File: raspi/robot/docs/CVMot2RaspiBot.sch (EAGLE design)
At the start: 2 parts

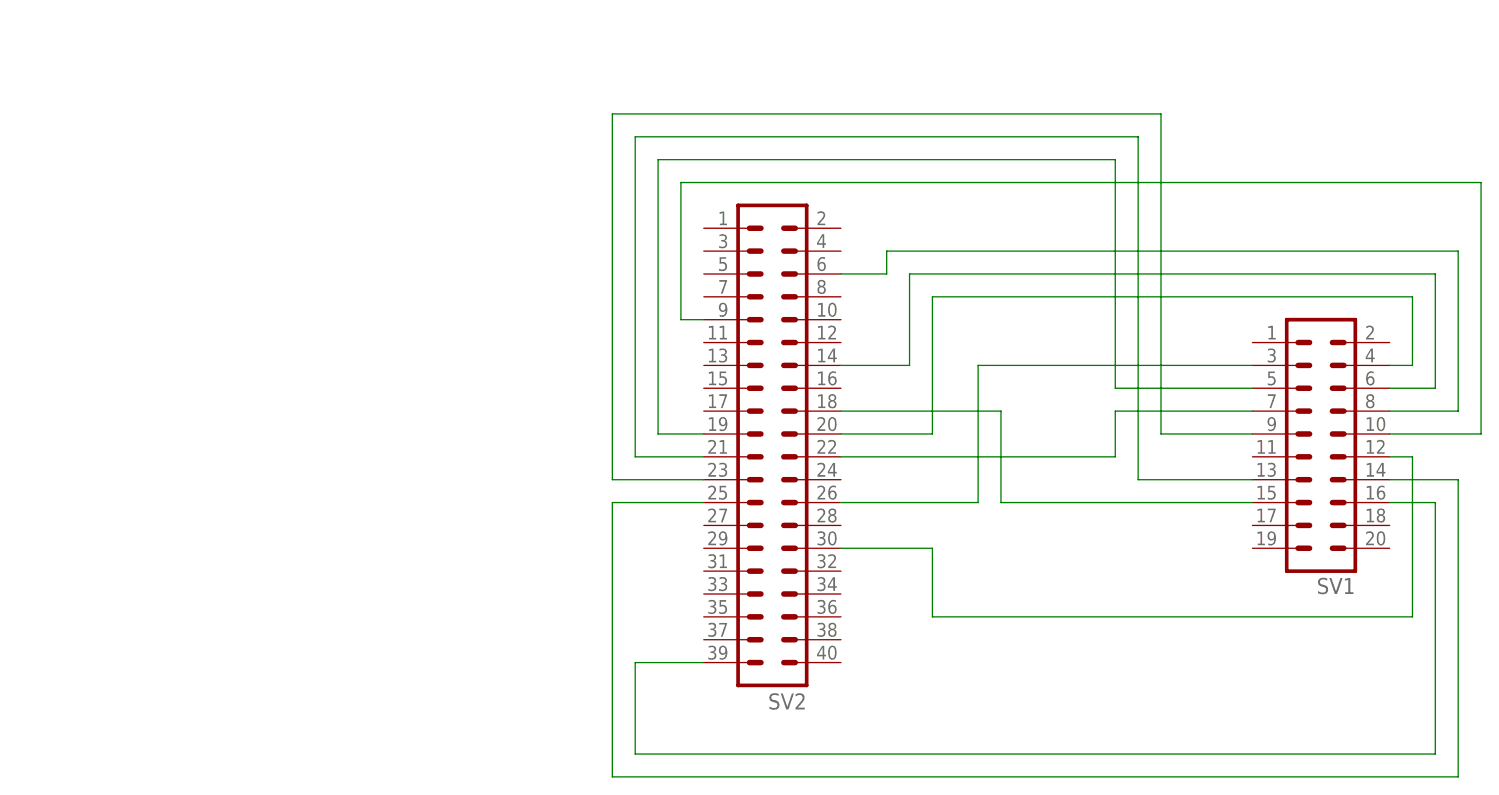
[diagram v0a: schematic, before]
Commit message: Raspi: Neue Adapter-Schaltpläne
git-svn-id: https://cvsvn/svn/raspi/trunk@92 50237d99-7d21-444e-87dd-016511c29f8c
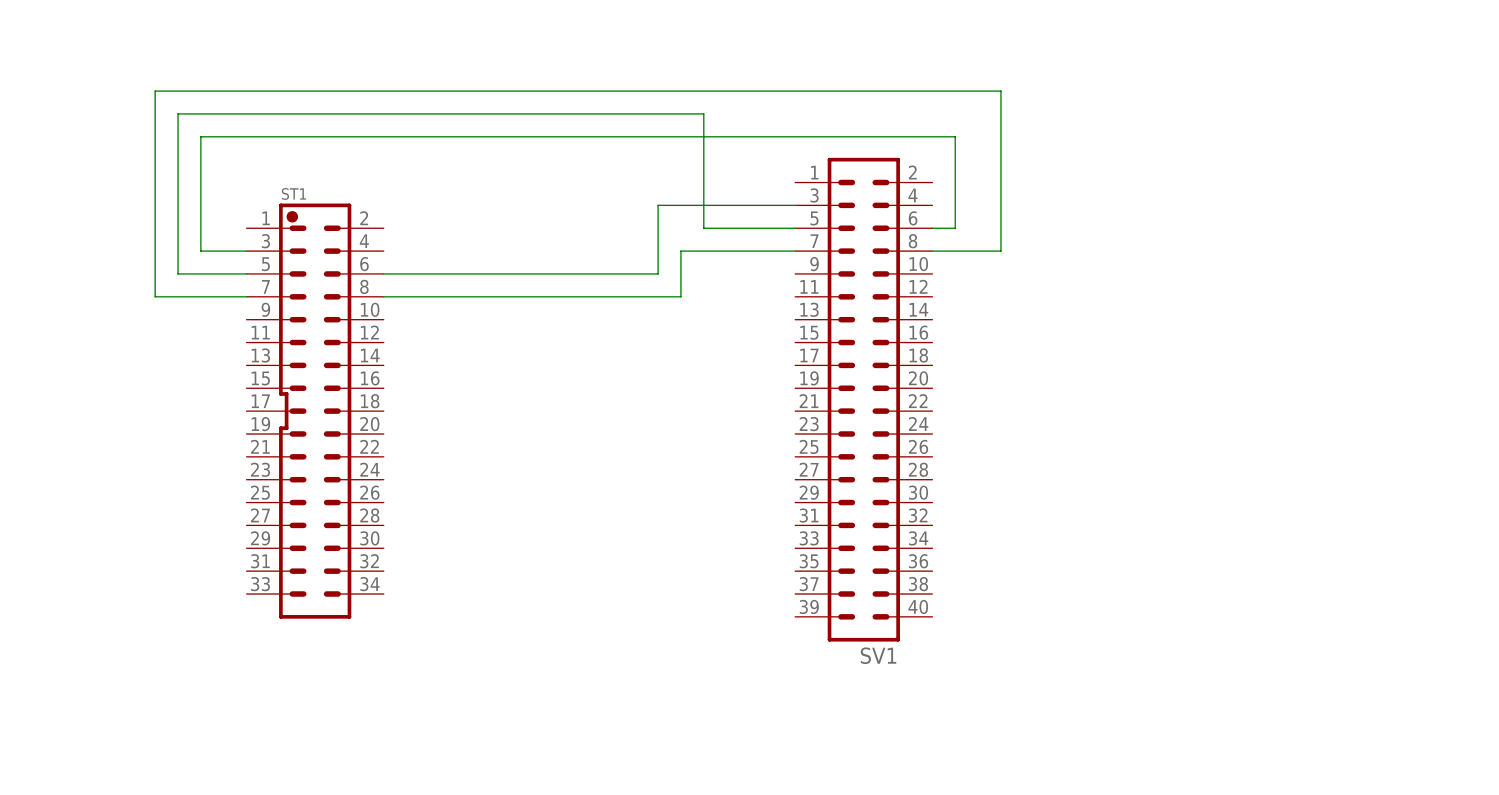
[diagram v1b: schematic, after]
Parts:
- removed SV2: (no value), con-harting-ml:ML40
- added ST1: (no value), CV_Con:STK-34-2R-MJST-PHD_34_TH
- SV1: device con-harting-ml:ML20 -> con-harting-ml:ML40
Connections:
- removed net GND: SV1.10, SV1.12, SV1.14, SV1.16, SV1.4, SV1.6, SV1.8, SV2.14, SV2.20, SV2.25, SV2.30, SV2.39, SV2.6, SV2.9
- removed net N$6: SV1.15, SV2.18
- net N$1: now also ST1.5; no longer SV2.19
- net N$2: now also ST1.6; no longer SV2.26
- net N$3: now also ST1.8; no longer SV2.22
- net N$4: now also ST1.7, SV1.8; no longer SV1.9, SV2.23
- net N$5: now also ST1.3, SV1.6; no longer SV1.13, SV2.21

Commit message: Raspi: Update Schaltpläne
git-svn-id: https://cvsvn/svn/raspi/trunk@93 50237d99-7d21-444e-87dd-016511c29f8c
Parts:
- removed SV1: (no value), con-harting-ml:ML40
- added ST2: B8B-PH-K-S, CV_Con:STK-08-1RJST-PH_8_TH
- added X1: RASPI_GPIO_B+#_PIN, raspberrypi_bastelstube_v13:RASPI_GPIO_B+#_PIN
- ST1: value (none) -> B26B-PHDSS; device CV_Con:STK-34-2R-MJST-PHD_34_TH -> CV_Con:STK-26-2RJST-PHD_26_TH
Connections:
- new net GND: ST1.25, ST1.26, ST1.3, ST1.4, ST2.3, X1.GND_A, X1.GND_B, X1.GND_C, X1.GND_D, X1.GND_E, X1.GND_F, X1.GND_G, X1.GND_H
- new net M1_CURRENT: ST1.6, X1.GPIO17
- new net M1_DIR: ST1.8, X1.GPIO27
- new net M1_STEP: ST1.7, X1.GPIO18
- new net MOTOR_RESET: ST1.5, X1.GPIO05
- new net N$10: ST1.19, X1.GPIO12
- new net N$11: ST1.20, X1.GPIO06
- new net N$19: ST2.4, X1.SPI_SCLK
- new net N$20: ST1.2, X1.5V0A
- new net N$21: ST1.1, ST2.2, X1.3V3A
- new net N$22: ST1.21, X1.SCL
- new net N$23: ST1.22, X1.SDA
- new net N$24: ST2.1, X1.5V0B
- new net N$27: ST2.5, X1.RXD
- new net N$28: ST2.6, X1.TXD
- new net N$29: ST2.7, X1.SPI_CE0
- new net N$30: ST2.8, X1.SPI_CE1
- new net N$6: ST1.13, X1.GPIO24
- new net N$7: ST1.15, X1.GPIO20
- new net N$8: ST1.17, X1.GPIO26
- new net N$9: ST1.16, X1.GPIO21
- net N$1: now also ST1.9, X1.GPIO13; no longer ST1.5, SV1.5
- net N$2: now also ST1.11, X1.GPIO16; no longer ST1.6, SV1.3
- net N$3: now also ST1.10, X1.GPIO19; no longer ST1.8, SV1.7
- net N$4: now also ST1.12, X1.GPIO22; no longer ST1.7, SV1.8
- net N$5: now also ST1.14, X1.GPIO23; no longer ST1.3, SV1.6
